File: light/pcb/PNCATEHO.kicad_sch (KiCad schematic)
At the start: 49 parts, among them J1 USB_C_Receptacle_USB2.0, SW11 Boot, SW12 Reset, U1 RP2040, U2 RT9013-33GB, U3 W25Q32JVSSIQ, Y1 12MHz

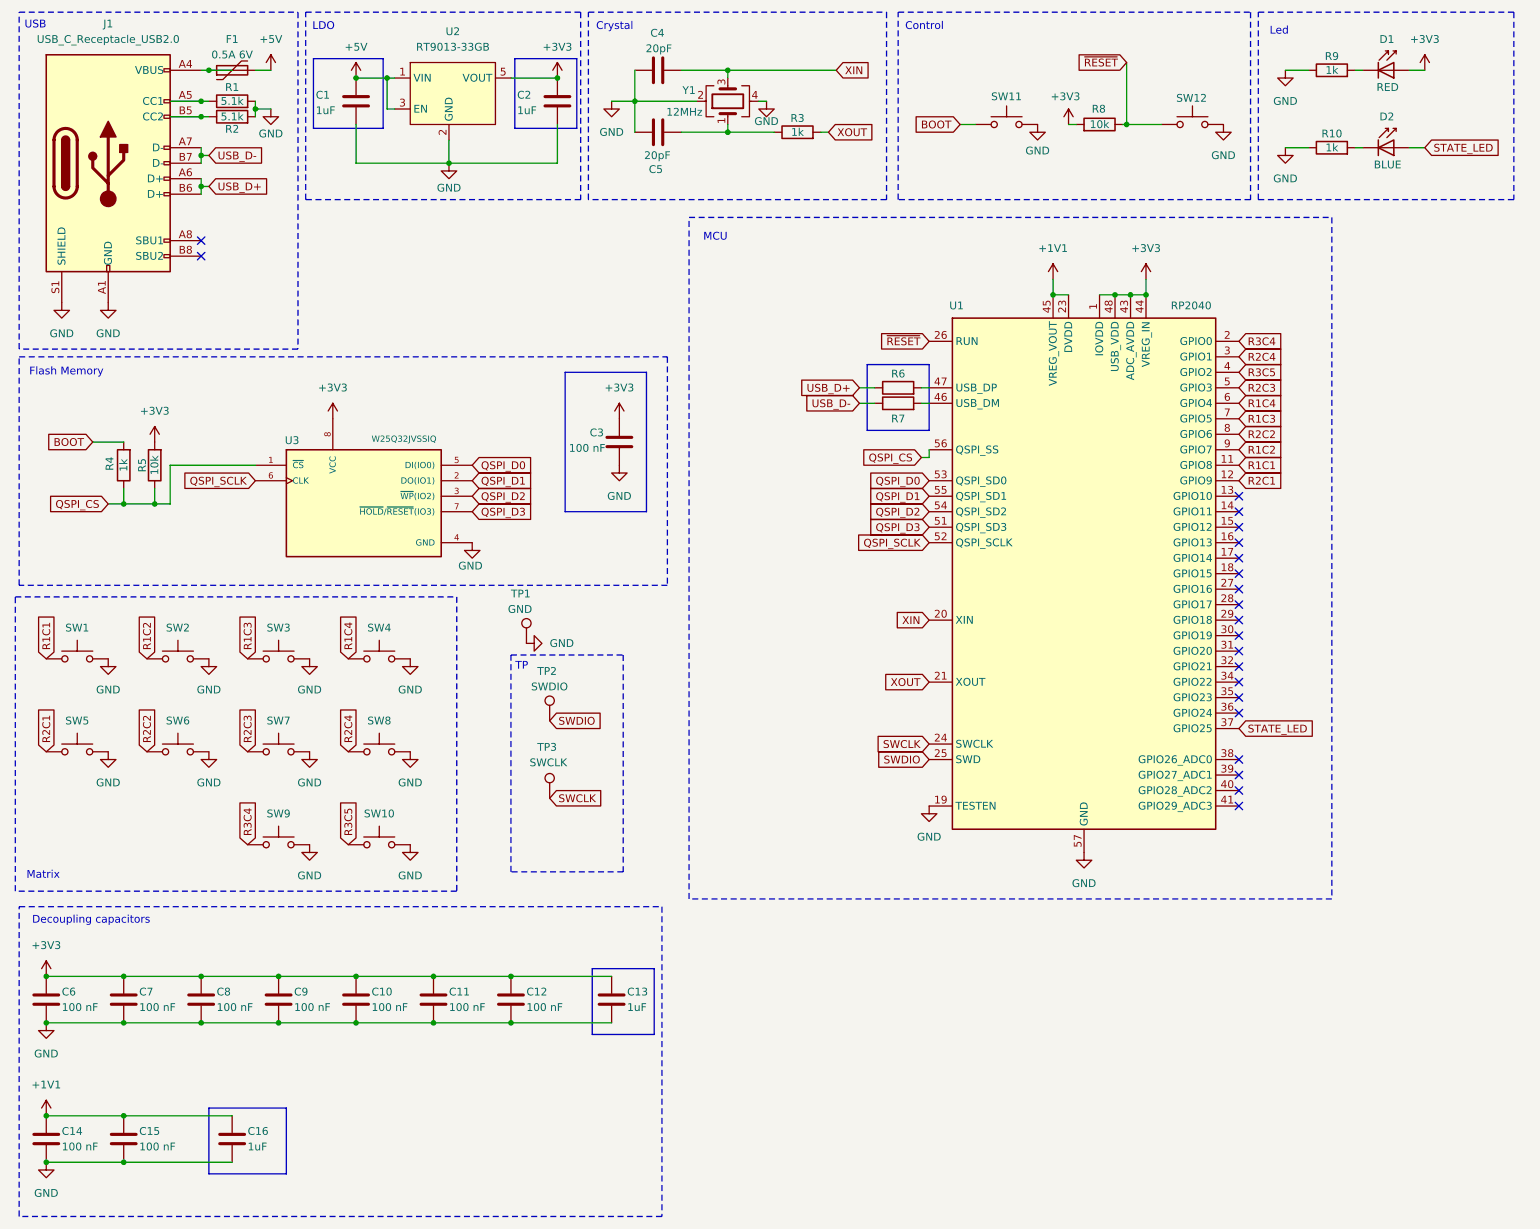
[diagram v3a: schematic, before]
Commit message: add esd protection
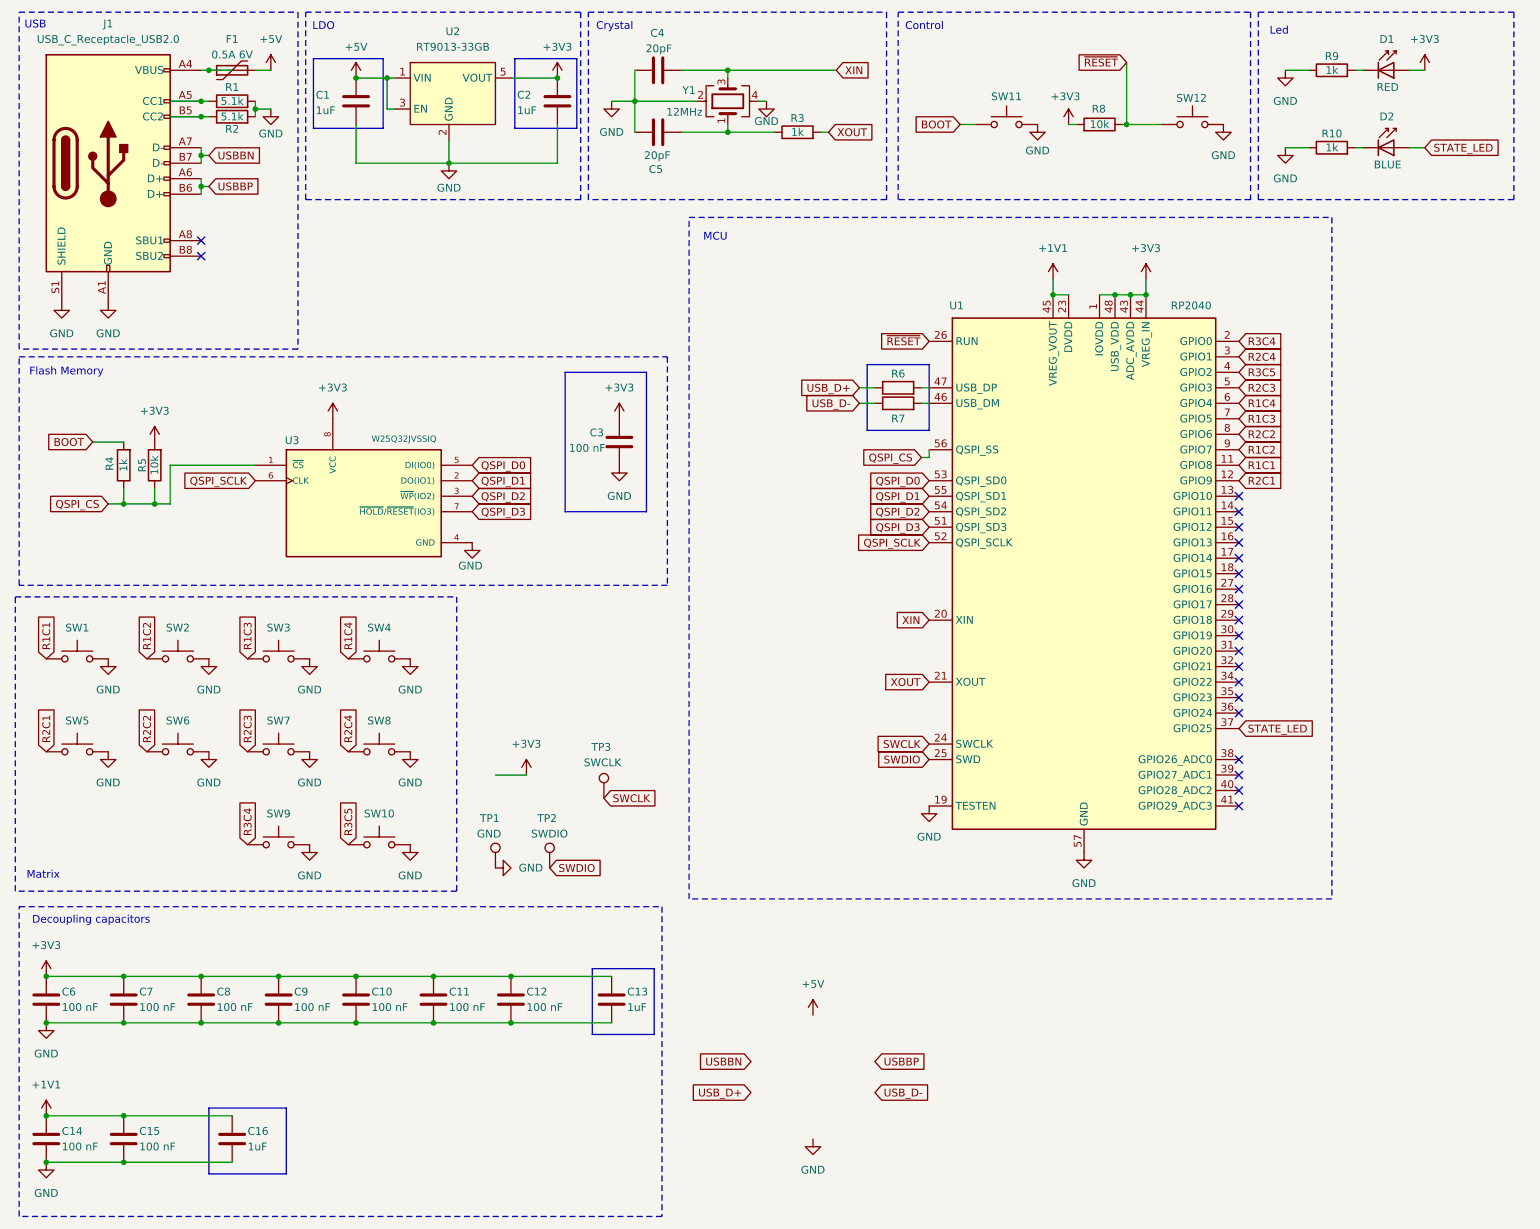
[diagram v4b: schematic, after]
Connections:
- net USB_D+: no longer J1.A6 (D+), J1.B6 (D+)
- net USB_D-: no longer J1.A7 (D-), J1.B7 (D-)
- new net USBBN: J1.A7 (D-), J1.B7 (D-)
- new net USBBP: J1.A6 (D+), J1.B6 (D+)
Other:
- note removed: "TP"
- moved on the sheet: TP1, TP2, TP3

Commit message: add some fix
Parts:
- added TP4: 3.3, PNCATEHO:TestPoint_Pad_D2.0mm, symbol PNCATEHO:TestPoint
- added U4: USBLC6-2SC6, PNCATEHO:SOT-23-6_Handsoldering_REV, symbol PNCATEHO:USBLC6-2SC6
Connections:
- net +3V3: now also TP4.1
- net +5V: now also U4.5 (VBUS)
- net GND: now also U4.2 (GND)
- net USBBN: now also U4.6 (I/O1)
- net USBBP: now also U4.4 (I/O2)
- net USB_D+: now also U4.1 (I/O1)
- net USB_D-: now also U4.3 (I/O2)
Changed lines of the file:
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@@
 	(wire
 		(pts
+			(xy 135.89 187.96) (xy 137.16 187.96)
+		)
+		(stroke
+			(width 0)
+			(type default)
+		)
+	)
+	(wire
+		(pts
 			(xy 41.91 90.17) (xy 55.88 90.17)
 		)
@@
 	(wire
 		(pts
+			(xy 147.32 177.8) (xy 147.32 180.34)
+		)
+		(stroke
+			(width 0)
+			(type default)
+		)
+	)
+	(wire
+		(pts
 			(xy 46.99 44.45) (xy 46.99 45.72)
 		)
@@
 	(wire
 		(pts
+			(xy 158.75 193.04) (xy 157.48 193.04)
+		)
+		(stroke
+			(width 0)
+			(type default)
+		)
+	)
+	(wire
+		(pts
+			(xy 158.75 187.96) (xy 157.48 187.96)
+		)
+		(stroke
+			(width 0)
+			(type default)
+		)
+	)
+	(wire
+		(pts
 			(xy 224.79 25.4) (xy 228.6 25.4)
 		)
@@
 	(global_label "USB_D-"
 		(shape input)
-		(at 157.48 193.04 0)
+		(at 158.75 193.04 0)
 		(fields_autoplaced yes)
 		(effects
@@
 		)
 		(property "Intersheetrefs" "${INTERSHEET_REFS}"
-			(at 168.0852 193.04 0)
+			(at 169.3552 193.04 0)
 			(effects
 				(font
@@
 	(global_label "USBBN"
 		(shape input)
-		(at 137.16 187.96 180)
+		(at 135.89 187.96 180)
 		(fields_autoplaced yes)
 		(effects
@@
 		)
 		(property "Intersheetrefs" "${INTERSHEET_REFS}"
-			(at 127.7643 187.96 0)
+			(at 126.4943 187.96 0)
 			(effects
 				(font
@@
 	(global_label "USBBP"
 		(shape input)
-		(at 157.48 187.96 0)
+		(at 158.75 187.96 0)
 		(fields_autoplaced yes)
 		(effects
@@
 		)
 		(property "Intersheetrefs" "${INTERSHEET_REFS}"
-			(at 166.8152 187.96 0)
+			(at 168.0852 187.96 0)
 			(effects
 				(font
@@
 	)
 	(symbol
+		(lib_id "PNCATEHO:USBLC6-2SC6")
+		(at 147.32 190.5 0)
+		(unit 1)
+		(exclude_from_sim no)
+		(in_bom yes)
+		(on_board yes)
+		(dnp no)
+		(fields_autoplaced yes)
+		(property "Reference" "U4"
+			(at 148.9711 177.8 0)
+			(effects
+				(font
+					(size 1.27 1.27)
+				)
+				(justify left)
+			)
+		)
+		(property "Value" "USBLC6-2SC6"
+			(at 148.9711 180.34 0)
+			(effects
+				(font
+					(size 1.27 1.27)
+				)
+				(justify left)
+			)
+		)
+		(property "Footprint" "PNCATEHO:SOT-23-6_Handsoldering_REV"
+			(at 147.32 203.2 0)
+			(effects
+				(font
+					(size 1.27 1.27)
+				)
+				(hide yes)
+			)
+		)
+		(property "Datasheet" "https://www.st.com/resource/en/datasheet/usblc6-2.pdf"
+			(at 152.4 181.61 0)
+			(effects
+				(font
+					(size 1.27 1.27)
+				)
+				(hide yes)
+			)
+		)
+		(property "Description" "Very low capacitance ESD protection diode, 2 data-line, SOT-23-6"
+			(at 147.32 190.5 0)
+			(effects
+				(font
+					(size 1.27 1.27)
+				)
+				(hide yes)
+			)
+		)
+		(pin "1"
+		)
+		(pin "4"
+		)
+		(pin "2"
+		)
+		(pin "6"
+		)
+		(pin "5"
+		)
+		(pin "3"
+		)
+		(instances
+			(project ""
+				(path "/02fc811b-599c-42c6-9c96-ff4b46846544"
+					(reference "U4")
+					(unit 1)
+				)
+			)
+		)
+	)
+	(symbol
 		(lib_id "PNCATEHO:C")
 		(at 97.79 177.8 0)
@@
 	(symbol
 		(lib_id "PNCATEHO:+5V")
-		(at 147.32 180.34 0)
+		(at 147.32 177.8 0)
 		(unit 1)
 		(exclude_from_sim no)
@@
 		(fields_autoplaced yes)
 		(property "Reference" "#PWR021"
-			(at 147.32 184.15 0)
+			(at 147.32 181.61 0)
 			(effects
 				(font
@@
 		)
 		(property "Value" "+5V"
-			(at 147.32 175.26 0)
+			(at 147.32 172.72 0)
 			(effects
 				(font
@@
 		)
 		(property "Footprint" ""
-			(at 147.32 180.34 0)
+			(at 147.32 177.8 0)
 			(effects
 				(font
@@
 		)
 		(property "Datasheet" ""
-			(at 147.32 180.34 0)
+			(at 147.32 177.8 0)
 			(effects
 				(font
@@
 		)
 		(property "Description" "Power symbol creates a global label with name \"+5V\""
-			(at 147.32 180.34 0)
+			(at 147.32 177.8 0)
 			(effects
 				(font
@@
 					(unit 1)
 				)
+			)
+		)
+	)
+	(symbol
+		(lib_id "PNCATEHO:TestPoint")
+		(at 95.25 140.97 0)
+		(unit 1)
+		(exclude_from_sim no)
+		(in_bom yes)
+		(on_board yes)
+		(dnp no)
+		(property "Reference" "TP4"
+			(at 93.218 132.588 0)
+			(effects
+				(font
+					(size 1.27 1.27)
+				)
+				(justify left)
+			)
+		)
+		(property "Value" "3.3"
+			(at 91.948 135.1279 0)
+			(effects
+				(font
+					(size 1.27 1.27)
+				)
+				(justify left)
+			)
+		)
+		(property "Footprint" "PNCATEHO:TestPoint_Pad_D2.0mm"
+			(at 100.33 140.97 0)
+			(effects
+				(font
+					(size 1.27 1.27)
+				)
+				(hide yes)
+			)
+		)
+		(property "Datasheet" "~"
+			(at 100.33 140.97 0)
+			(effects
+				(font
+					(size 1.27 1.27)
+				)
+				(hide yes)
+			)
+		)
+		(property "Description" "test point"
+			(at 95.25 140.97 0)
+			(effects
+				(font
+					(size 1.27 1.27)
+				)
+				(hide yes)
+			)
+		)
+		(pin "1"
+		)
+		(instances
+			(project "PNCATEHO"
+				(path "/02fc811b-599c-42c6-9c96-ff4b46846544"
+					(reference "TP4")
+					(unit 1)
+				)

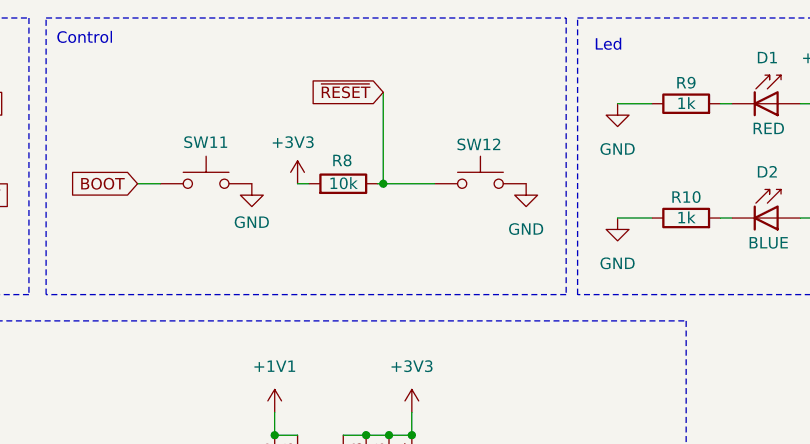
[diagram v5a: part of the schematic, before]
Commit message: remove reset button
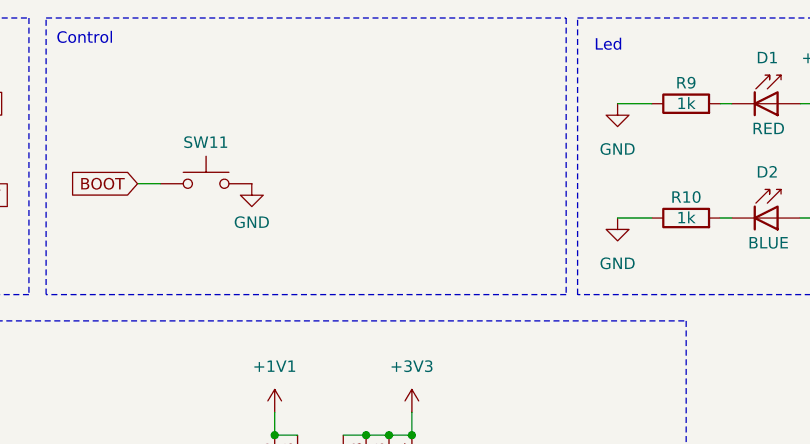
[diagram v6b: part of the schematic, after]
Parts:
- removed R8: 10k, PNCATEHO:R_0805_2012Metric_Pad1.20x1.40mm_HandSolder, symbol PNCATEHO:R
- removed SW12: Reset, PNCATEHO:SW_SMD_L4_W3_H1.5, symbol PNCATEHO:SW_Push

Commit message: remove led
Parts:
- removed D1: RED, PNCATEHO:LED_0805_2012Metric_Pad1.15x1.40mm_HandSolder, symbol PNCATEHO:D_Generic
- removed D2: BLUE, PNCATEHO:LED_0805_2012Metric_Pad1.15x1.40mm_HandSolder, symbol PNCATEHO:D_Generic
- removed R10, R9: 1k, PNCATEHO:R_0805_2012Metric_Pad1.20x1.40mm_HandSolder, symbol PNCATEHO:R
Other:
- note removed: "Led"

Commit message: fix
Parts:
- added D1: Red, PNCATEHO:D_0805_2012Metric_Pad1.15x1.40mm_HandSolder, symbol PNCATEHO:D_Generic
- added D2: Blue, PNCATEHO:D_0805_2012Metric_Pad1.15x1.40mm_HandSolder, symbol PNCATEHO:D_Generic
- added R10, R9: 1k, PNCATEHO:R_0805_2012Metric_Pad1.20x1.40mm_HandSolder, symbol PNCATEHO:R
- added R8: 10k, PNCATEHO:R_0805_2012Metric_Pad1.20x1.40mm_HandSolder, symbol PNCATEHO:R
- added SW12: Boot, PNCATEHO:PADS, symbol PNCATEHO:SW_Push
- SW11: footprint PNCATEHO:SW_SMD_L4_W3_H1.5 -> PNCATEHO:PADS
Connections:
- net +3V3: now also D1.2 (A), R8.1
- net GND: now also R10.1, R9.1, SW12.1
- net STATE_LED: now also D2.2 (A)
- new net: D1.1 (K), R9.2
- new net: R8.2, SW12.2
- new net: D2.1 (K), R10.2
